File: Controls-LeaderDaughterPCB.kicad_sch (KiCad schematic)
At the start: 10 parts

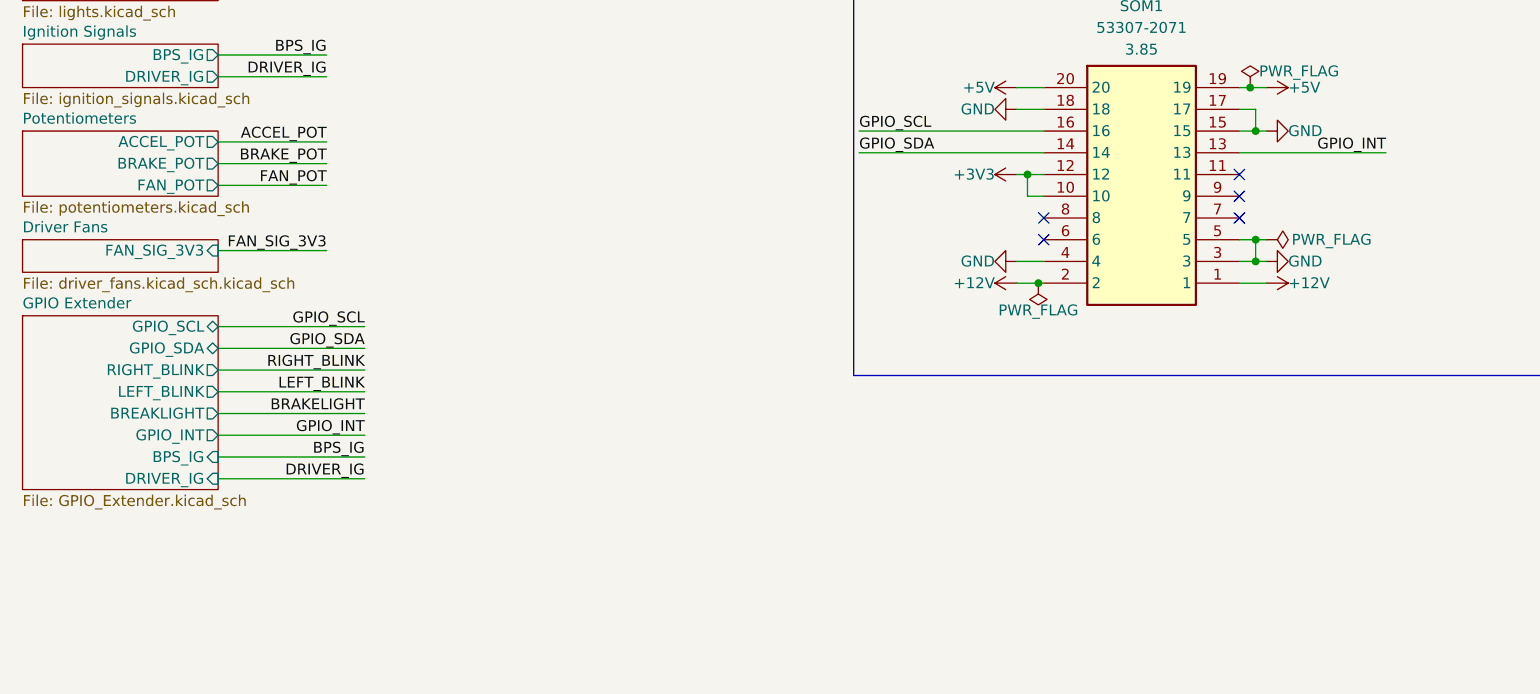
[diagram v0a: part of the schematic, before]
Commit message: Organized schematic, added reset function to extender, changed footprints
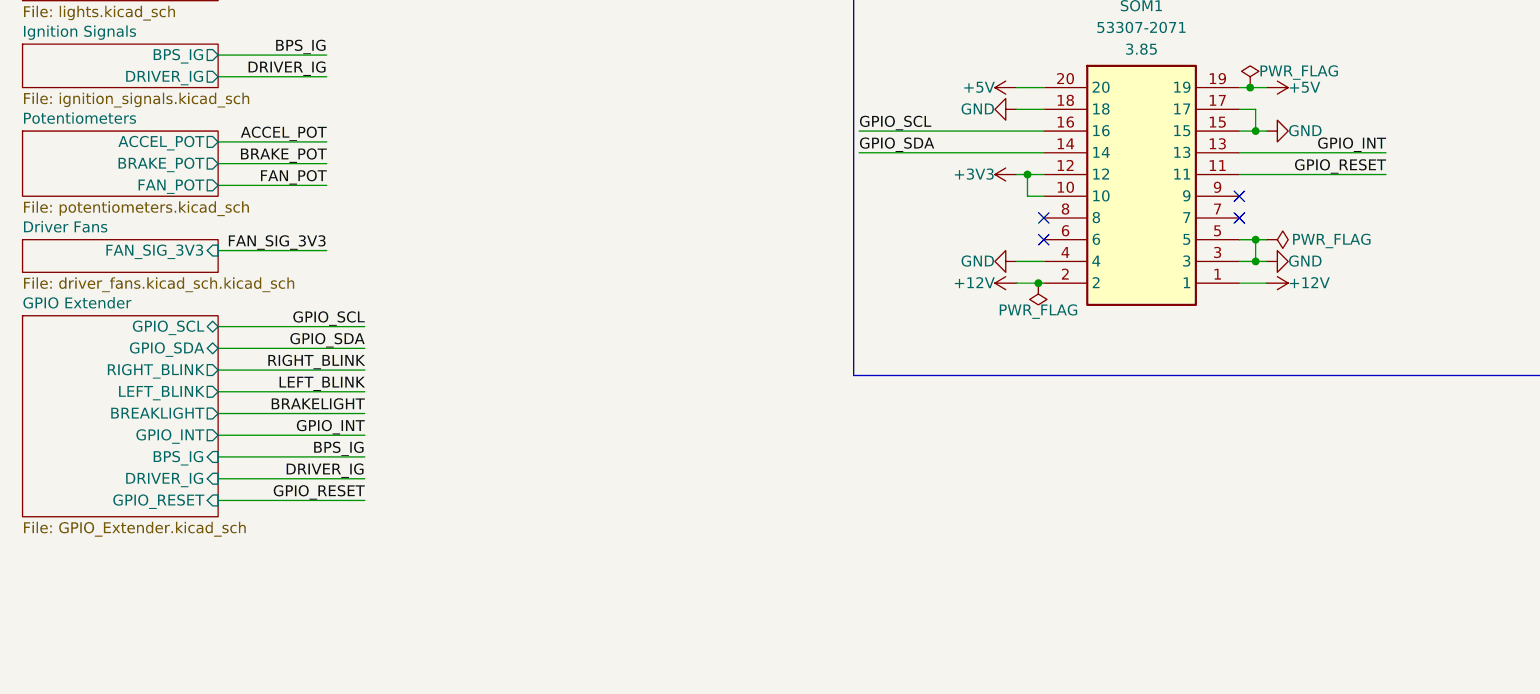
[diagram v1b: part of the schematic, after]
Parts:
- SOM1, SOM2: footprint UTSVT_Special:PeripheralSOM -> UTSVT_Connectors:Molex_53307-2071
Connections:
- net GPIO_RESET: now reaches SOM1.11
- no-connect marks 7 -> 6
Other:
- sheet GPIO Extender ports: added GPIO_RESET; removed none
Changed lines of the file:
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@@
   (no_connect (at 248.92 48.895))
   (no_connect (at 154.94 45.085))
-  (no_connect (at 154.94 42.545))
   (no_connect (at 132.08 50.165))
   (no_connect (at 132.08 47.625))
@@
     (stroke (width 0) (type default))
   )
+  (wire (pts (xy 154.94 42.545) (xy 172.085 42.545))
+    (stroke (width 0) (type default))
+  )
   (wire (pts (xy 224.155 33.655) (xy 224.155 36.195))
     (stroke (width 0) (type default))
@@
   )
   (wire (pts (xy 110.49 40.005) (xy 132.08 40.005))
+    (stroke (width 0) (type default))
+  )
+  (wire (pts (xy 35.56 80.645) (xy 52.705 80.645))
     (stroke (width 0) (type default))
   )
@@
     (effects (font (size 4 4) (thickness 0.8) bold) (justify left bottom))
   )
+  (label "GPIO_RESET" (at 172.085 42.545 180) (fields_autoplaced)
+    (effects (font (size 1.27 1.27)) (justify right bottom))
+  )
   (label "RIGHT_BLINK" (at 52.705 65.405 180) (fields_autoplaced)
     (effects (font (size 1.27 1.27)) (justify right bottom))
@@
   (label "ACCEL_POT" (at 204.47 38.735 0) (fields_autoplaced)
     (effects (font (size 1.27 1.27)) (justify left bottom))
+  )
+  (label "GPIO_RESET" (at 52.705 80.645 180) (fields_autoplaced)
+    (effects (font (size 1.27 1.27)) (justify right bottom))
   )
   (label "DRIVER_IG" (at 48.26 31.115 180) (fields_autoplaced)
@@
       (effects (font (size 1.27 1.27)))
     )
-    (property "Footprint" "UTSVT_Special:PeripheralSOM" (at 237.49 28.575 0)
+    (property "Footprint" "UTSVT_Connectors:Molex_53307-2071" (at 237.49 28.575 0)
       (effects (font (size 1.27 1.27)) hide)
     )
@@
       (effects (font (size 1.27 1.27)))
     )
-    (property "Footprint" "UTSVT_Special:PeripheralSOM" (at 143.51 27.305 0)
+    (property "Footprint" "UTSVT_Connectors:Molex_53307-2071" (at 143.51 27.305 0)
       (effects (font (size 1.27 1.27)) hide)
     )
@@
     )
   )
-  (sheet (at 12.7 59.055) (size 22.86 20.32) (fields_autoplaced)
+  (sheet (at 12.7 59.055) (size 22.86 23.495) (fields_autoplaced)
     (stroke (width 0.1524) (type solid))
     (fill (color 0 0 0 0.0000))
@@
       (effects (font (size 1.27 1.27)) (justify left bottom))
     )
-    (property "Sheetfile" "GPIO_Extender.kicad_sch" (at 12.7 79.9596 0)
+    (property "Sheetfile" "GPIO_Extender.kicad_sch" (at 12.7 83.1346 0)
       (effects (font (size 1.27 1.27)) (justify left top))
     )
@@
       (effects (font (size 1.27 1.27)) (justify right))
     )
+    (pin "GPIO_RESET" input (at 35.56 80.645 0)
+      (effects (font (size 1.27 1.27)) (justify right))
+    )

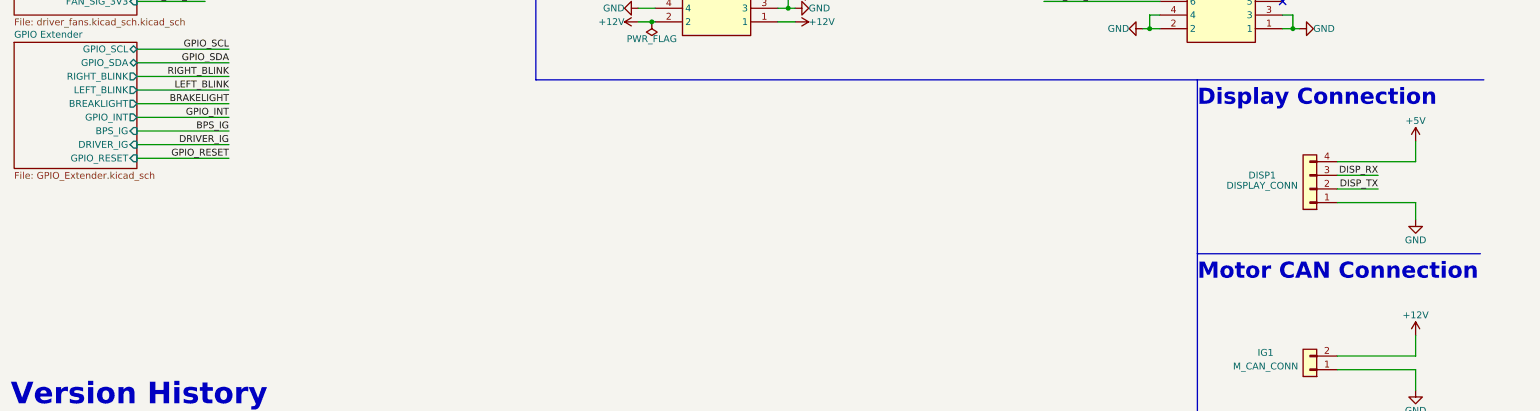
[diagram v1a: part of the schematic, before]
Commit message: added notes section to bottom of sheets
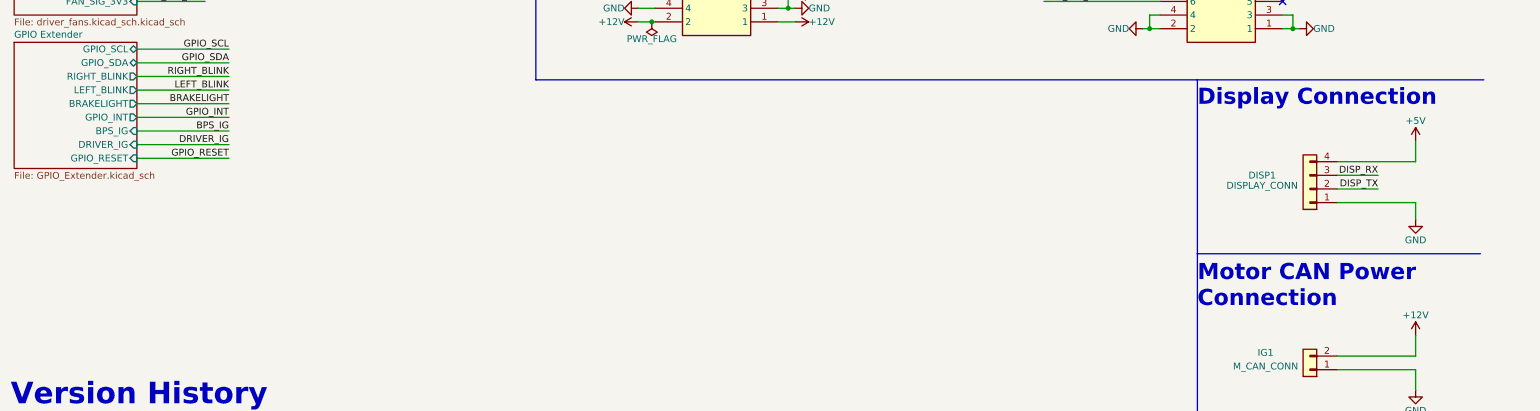
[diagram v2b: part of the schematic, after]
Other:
- sheet GPIO Extender ports: added BRAKELIGHT; removed BREAKLIGHT
- note added: "Motor CAN Power Connection"
- note removed: "Motor CAN Connection"
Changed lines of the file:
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@@
     (effects (font (size 1.27 1.27) bold) (justify left bottom))
   )
-  (text "Motor CAN Connection\n" (at 233.045 103.505 0)
+  (text "Motor CAN Power\nConnection\n" (at 233.045 108.585 0)
     (effects (font (size 3 3) (thickness 0.7) bold) (justify left bottom))
   )
@@
       (effects (font (size 1.27 1.27)) (justify right))
     )
-    (pin "BREAKLIGHT" output (at 35.56 70.485 0)
-      (effects (font (size 1.27 1.27)) (justify right))
-    )
+    (pin "BRAKELIGHT" output (at 35.56 70.485 0)
+      (effects (font (size 1.27 1.27)) (justify right))
+    )
